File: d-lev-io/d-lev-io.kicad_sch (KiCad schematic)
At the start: 28 parts, among them J1 USB_C_Receptacle_USB2.0, J2 PJ-059A, J3 Conn_01x12_MountingPin, J4 MIDI_OUT_JACK, U6 74AHC1G126

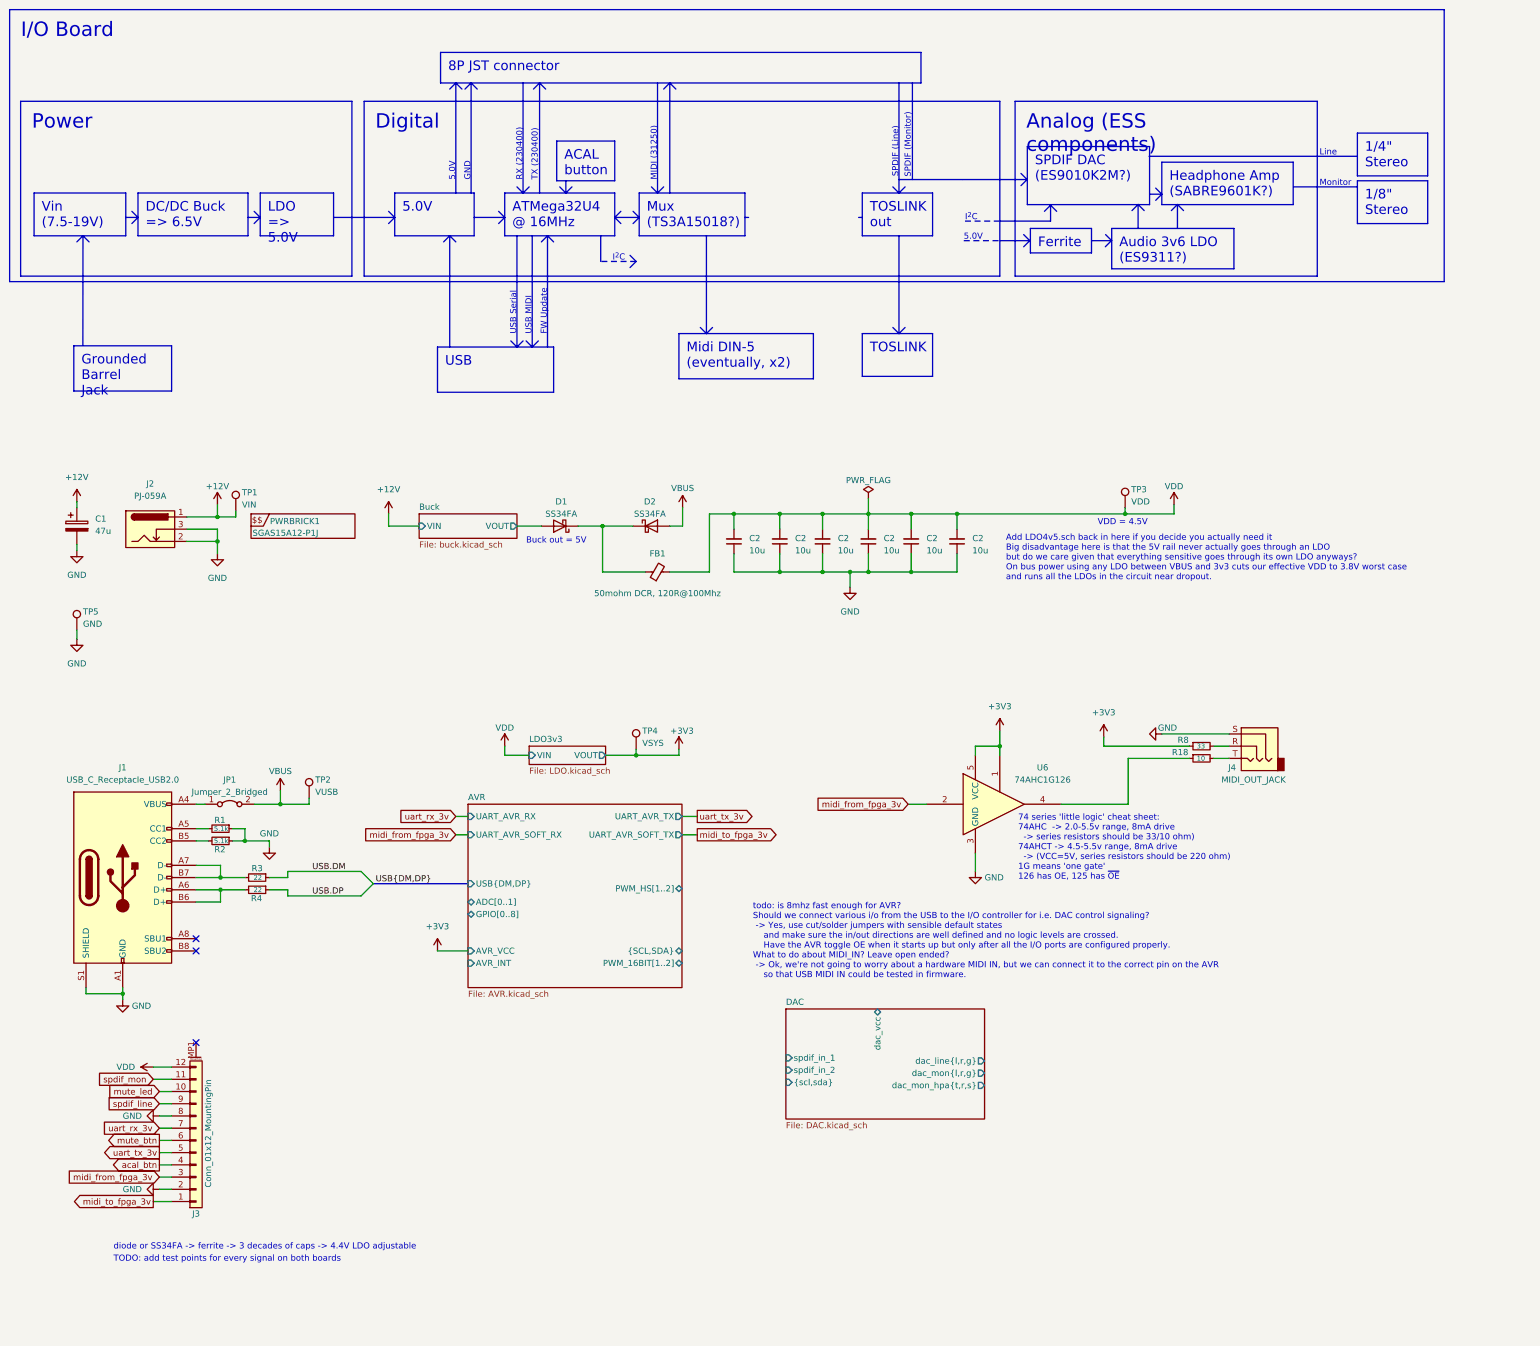
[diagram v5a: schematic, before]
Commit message: map SAMD21 pins
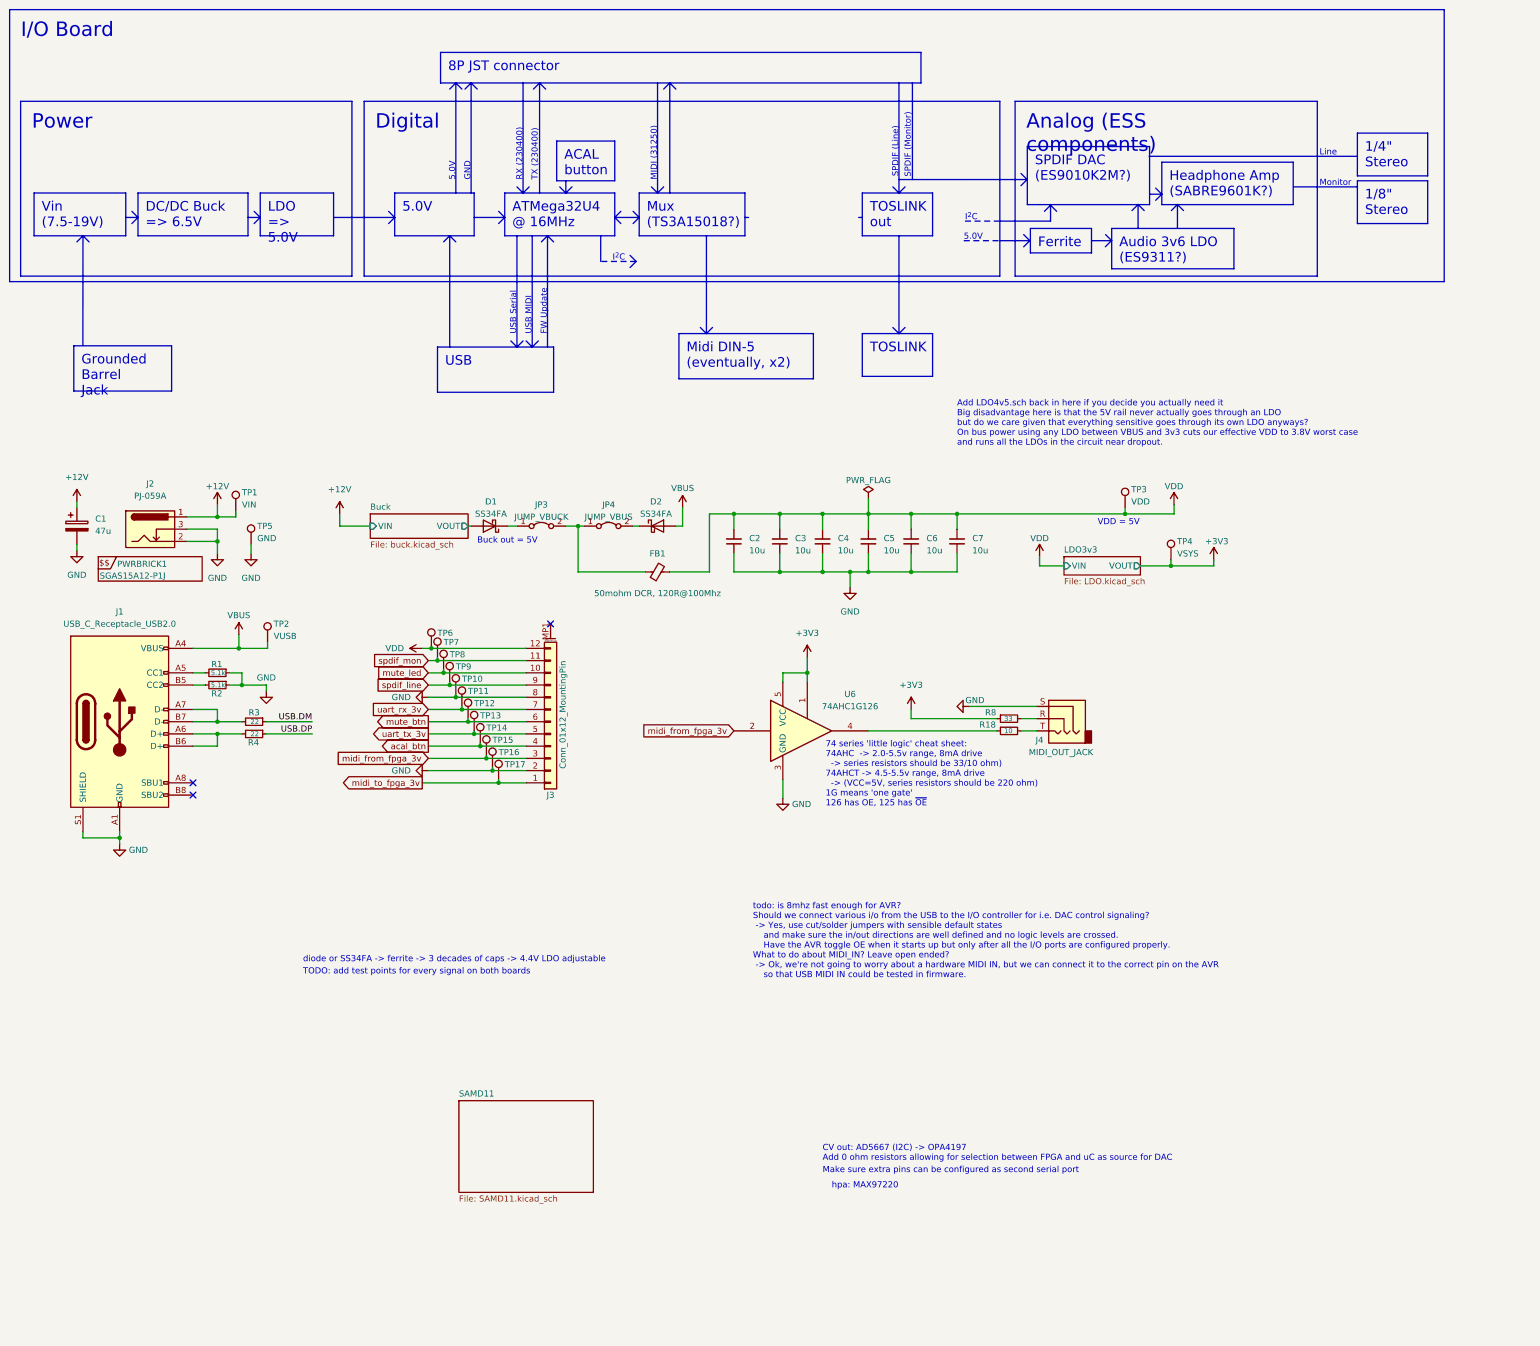
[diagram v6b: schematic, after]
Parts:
- removed JP1: Jumper_2_Bridged, Jumper:SolderJumper-2_P1.3mm_Bridged_RoundedPad1.0x1.5mm, symbol Jumper:Jumper_2_Bridged
- added JP3: JUMP_VBUCK, Jumper:SolderJumper-2_P1.3mm_Bridged_RoundedPad1.0x1.5mm, symbol Jumper:Jumper_2_Bridged
- added JP4: JUMP_VBUS, Jumper:SolderJumper-2_P1.3mm_Bridged_RoundedPad1.0x1.5mm, symbol Jumper:Jumper_2_Bridged
- added TP10, TP11, TP12, TP13, TP14, TP15, TP16, TP17, TP6, TP7, TP8, TP9: VUSB, TestPoint:TestPoint_Pad_D1.5mm, symbol Connector:TestPoint
- renumbered C2 to C3, C2 to C4, C2 to C5, C2 to C6, C2 to C7
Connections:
- net +5V: now also TP6.1
- net GND: now also TP10.1, TP16.1
- net VBUS: now also J1.A4 (VBUS), J1.A9 (VBUS), J1.B4 (VBUS), J1.B9 (VBUS)
- net acal_btn: now also TP14.1
- net midi_from_fpga_3v: now also TP15.1
- net midi_to_fpga_3v: now also TP17.1
- net mute_btn: now also TP12.1
- net mute_led: now also TP8.1
- net spdif_line: now also TP9.1
- net spdif_mon: now also TP7.1
- net uart_rx_3v: now also TP11.1
- net uart_tx_3v: now also TP13.1
- new net: D1.1 (K), JP3.1 (A)
- new net: FB1.1, JP3.2 (B), JP4.1 (A)
- new net: D2.1 (K), JP4.2 (B)
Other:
- removed sheet AVR
- removed sheet DAC
- added sheet SAMD11 (SAMD11.kicad_sch)
- note added: "CV out: AD5667 (I2C) -> OPA4197 Add 0 ohm resistors allowing for selection between FPGA and uC as source for DAC"
- note added: "Make sure extra pins can be configured as second serial port"
- note added: "VDD = 5V"
- note added: "hpa: MAX97220"
- note removed: "VDD = 4.5V"
- moved on the sheet: D1, D2, J1, J3, J4, PWRBRICK1, R1, R18, R2, R3, R4, R8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

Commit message: Added DAC schematic to I/O board
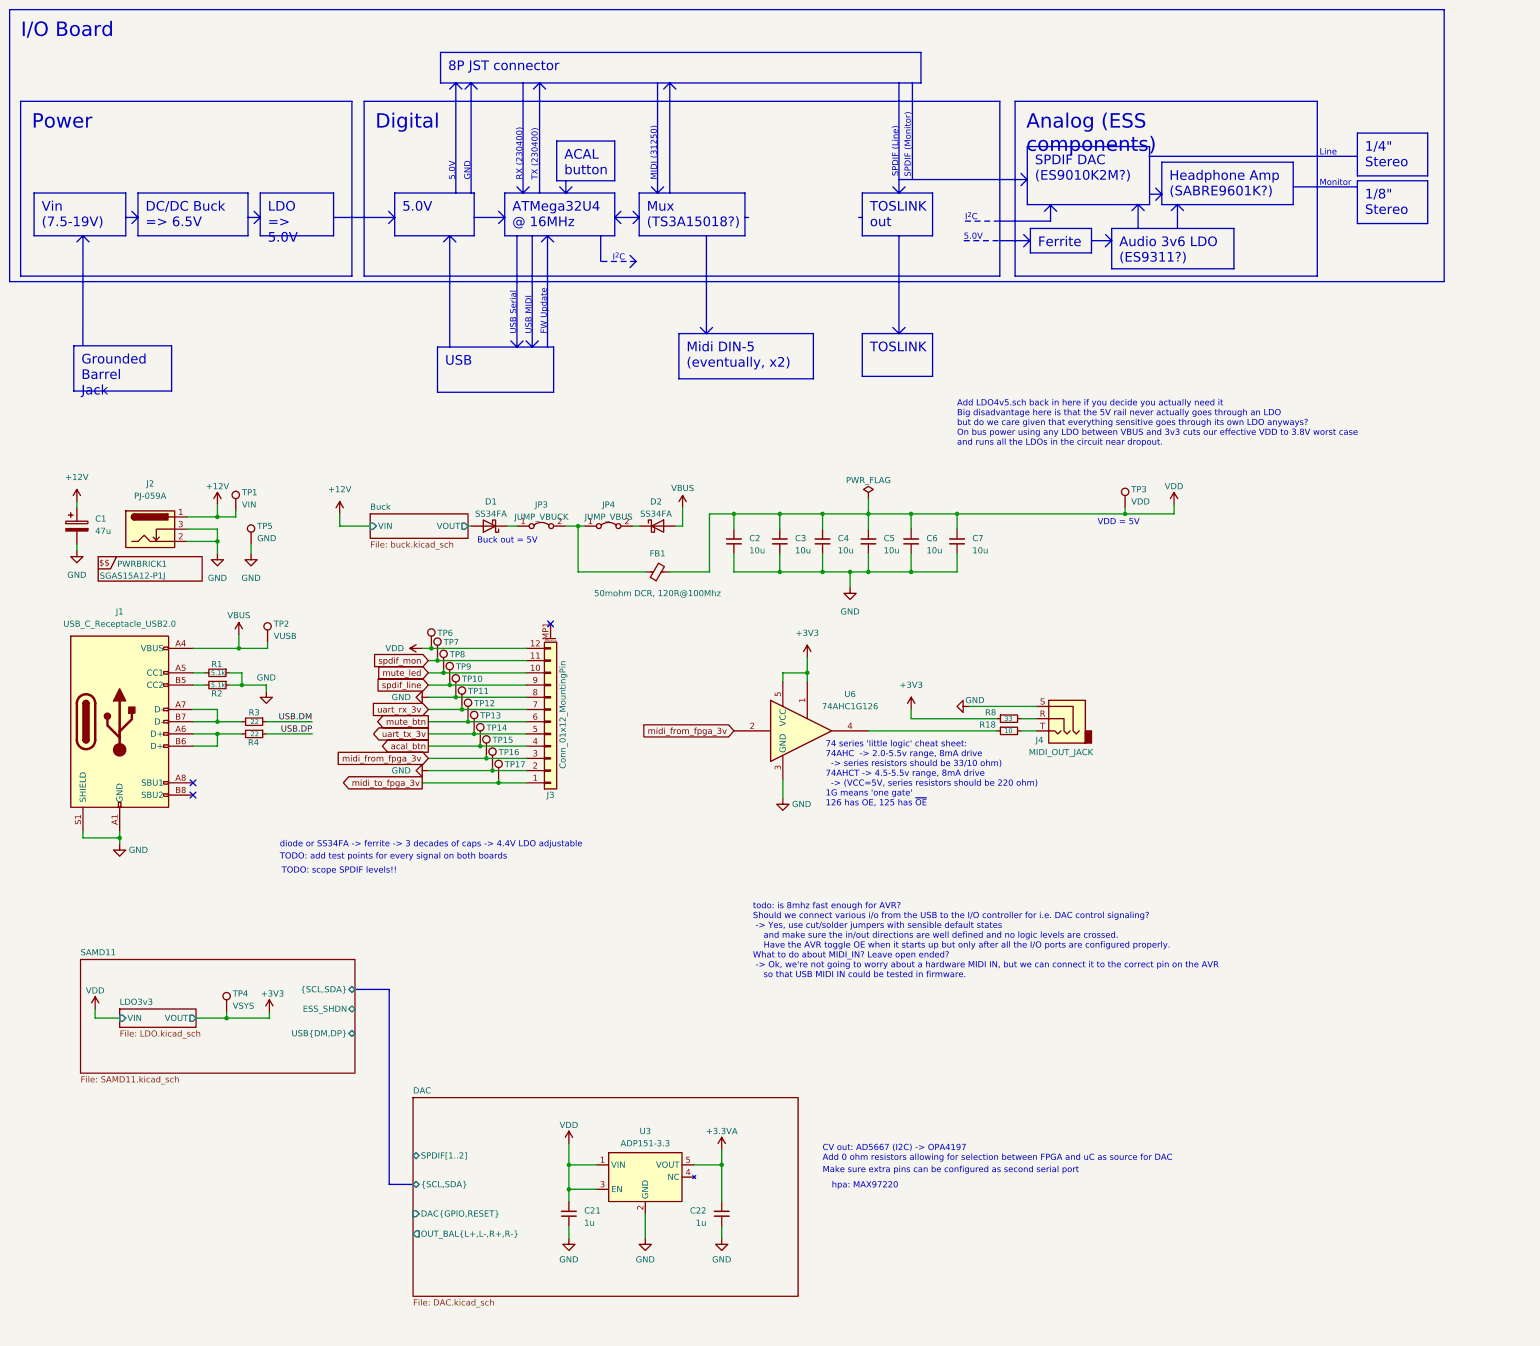
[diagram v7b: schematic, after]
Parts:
- added C21, C22: 1u, Capacitor_SMD:C_0603_1608Metric, symbol Device:C_Small
- added U3: ADP151-3.3, Package_TO_SOT_SMD:TSOT-23-5, symbol ess_dac:ADP151-3.3
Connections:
- net GND: now also C21.1, C22.1, U3.2 (GND)
- new net +3.3VA: C22.2, U3.5 (VOUT)
- new net VDD: C21.2, U3.1 (VIN), U3.3 (EN)
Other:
- added sheet DAC (DAC.kicad_sch)
- sheet SAMD11 ports: added ESS_SHDN, USB{DM,DP}, {SCL,SDA}; removed none
- note added: "TODO: scope SPDIF levels!!"
- moved on the sheet: TP4

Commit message: add headphone amp
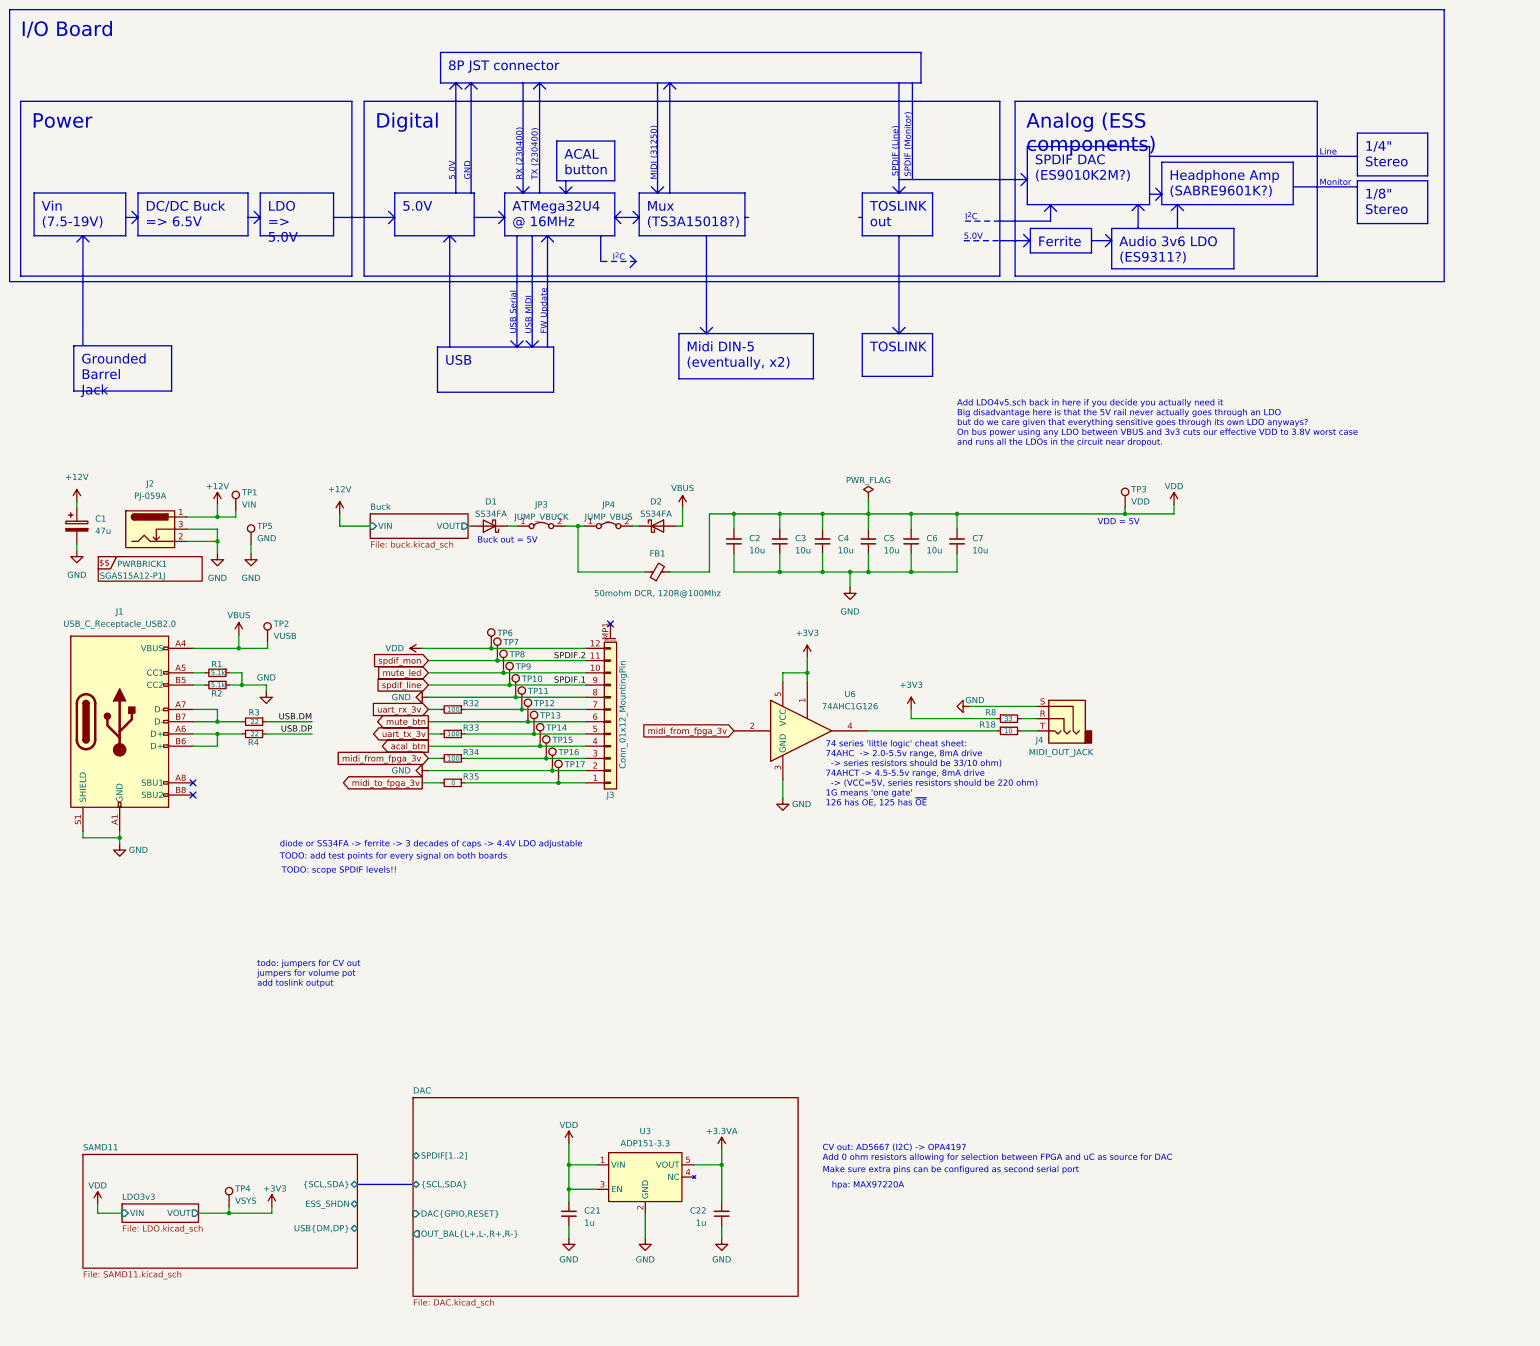
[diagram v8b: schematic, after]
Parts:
- added R32, R33, R34: 100, Resistor_SMD:R_0603_1608Metric, symbol Device:R_Small
- added R35: 0, Resistor_SMD:R_0603_1608Metric, symbol Device:R_Small
- U3: footprint Package_TO_SOT_SMD:TSOT-23-5 -> Package_TO_SOT_SMD:SOT-23-5
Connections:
- net midi_from_fpga_3v: now also R34.2; no longer J3.3 (Pin_3), TP15.1
- net midi_to_fpga_3v: now also R35.2; no longer J3.1 (Pin_1), TP17.1
- net uart_rx_3v: now also R32.2; no longer J3.7 (Pin_7), TP11.1
- net uart_tx_3v: now also R33.2; no longer J3.5 (Pin_5), TP13.1
- new net: J3.3 (Pin_3), R34.1, TP15.1
- new net: J3.5 (Pin_5), R33.1, TP13.1
- new net: J3.7 (Pin_7), R32.1, TP11.1
- new net: J3.1 (Pin_1), R35.1, TP17.1
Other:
- note added: "hpa: MAX97220A"
- note added: "todo: jumpers for CV out jumpers for volume pot add toslink output"
- note removed: "hpa: MAX97220"
- note removed: "todo: is 8mhz fast enough for AVR? Should we connect various i/o from the USB to the I/O controller for i.e. DAC control signaling? -> Yes, use cut/solder jumpers with sensible default states and make sure the in/out directions are well defined and no logic levels are crossed. Have the AVR toggle OE when it starts up but only after all the I/O ports are configured properly. What to do about MIDI_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"
- moved on the sheet: J3, TP10, TP11, TP12, TP13, TP14, TP15, TP16, TP17, TP4, TP6, TP7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
